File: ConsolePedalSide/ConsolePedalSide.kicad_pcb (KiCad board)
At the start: 2 copper layers, 93 x 31.6 mm, 18 parts, among them J1 AudioJack3, J2 AudioJack2, J3 SlotA, J4 SlotB

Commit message: Fixed footprints
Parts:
- removed the G*** at (133.6, 117.0) (x2)
- added G***: LOGO, libraries:consolePedalsLogo, F.Cu at (133.7, 117.9)
- added G***: LOGO, libraries:consolePedalsLogo, B.Cu at (133.7, 117.9)
- moved D1 1.80 mm to (117.1, 104.5), turned to 270 degrees
- moved D3 1.80 mm to (150.0, 104.5), turned to 270 degrees
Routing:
- net Net-(J2-Pad1): track 13.8 -> 21.4 mm
- net /SlotBLED: track 45.6 -> 39.6 mm
- net /SlotAInput: track 20.6 -> 18.4 mm
- net Net-(S1-PadP$5): track 65.8 -> 67.8 mm
- net Net-(D1-Pad1): track 4.97 -> 6.83 mm
- net Net-(D3-Pad1): track 4.97 -> 6.83 mm
- net /SlotBInput: track 19.3 -> 20.9 mm
- net /SlotALED: track 22.3 -> 23.4 mm
- net +9V: track 88.5 -> 89.4 mm
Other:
- board text added: "Console Pedal Side V1.1"
- board text removed: "Console Pedal Side V1.0"

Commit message: Switched input and output jack locations
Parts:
- moved J1 83.7 mm to (175.4, 108.5)
- moved J2 83.7 mm to (91.7, 109.8)
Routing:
- net Net-(J1-Pad3): track 7.57 -> 108.9 mm, vias 0 -> 1
- net Net-(J2-Pad1): track 21.4 -> 94.0 mm
- net Net-(BT1-Pad2): track 49.4 -> 57.6 mm
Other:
- board text added: "Console Pedal Side V1.2"
- board text removed: "Console Pedal Side V1.1"

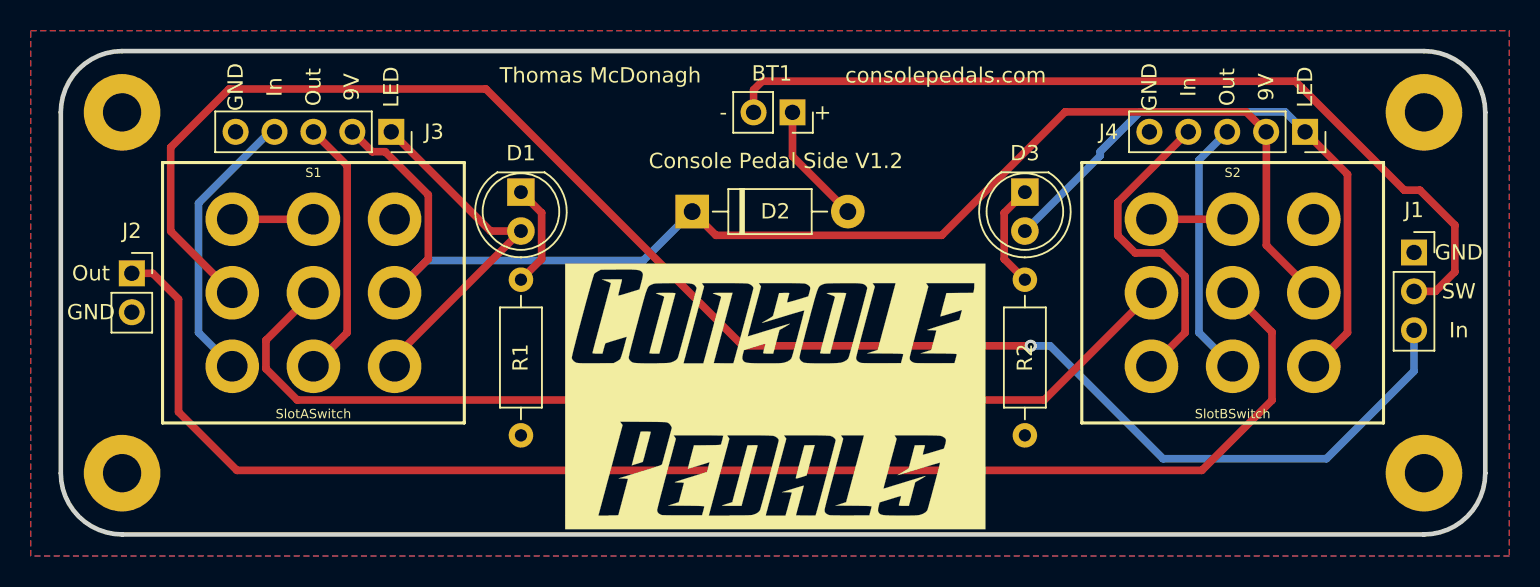
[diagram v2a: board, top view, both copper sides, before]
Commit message: Made pin holes wider for easier hand soldering
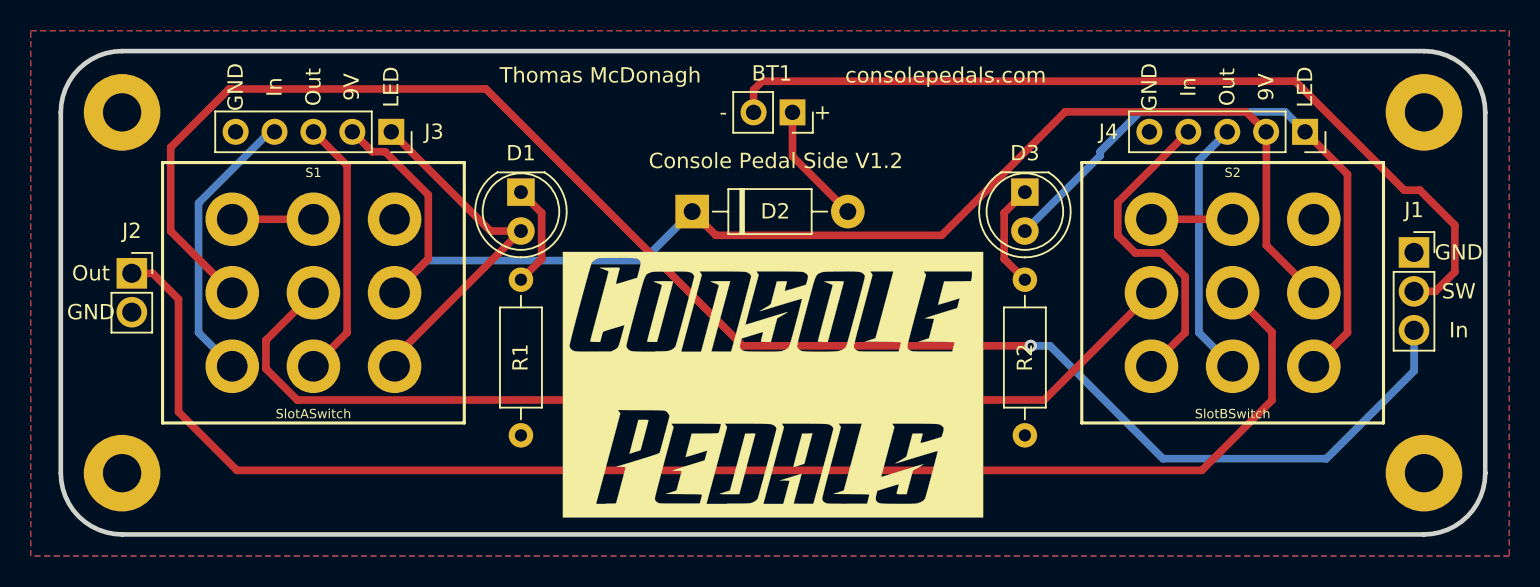
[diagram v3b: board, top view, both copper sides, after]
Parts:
- removed the G*** at (133.7, 117.9) (x2)
- added G***: LOGO, libraries:consolePedalsLogo, B.Cu at (133.5, 117.1)
- added G***: LOGO, libraries:consolePedalsLogo, F.Cu at (133.5, 117.1)
- J1: footprint Connector_PinSocket_2.54mm:PinSocket_1x03_P2.54mm_Vertical -> libraries:Pins_1x03_Wide
- J2: footprint Connector_PinSocket_2.54mm:PinSocket_1x02_P2.54mm_Vertical -> libraries:Pins_1x02_Wide
